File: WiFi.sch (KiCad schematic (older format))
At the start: 5 parts, among them J3 Flash enable, SW1 RESET, U9 ESP-12F

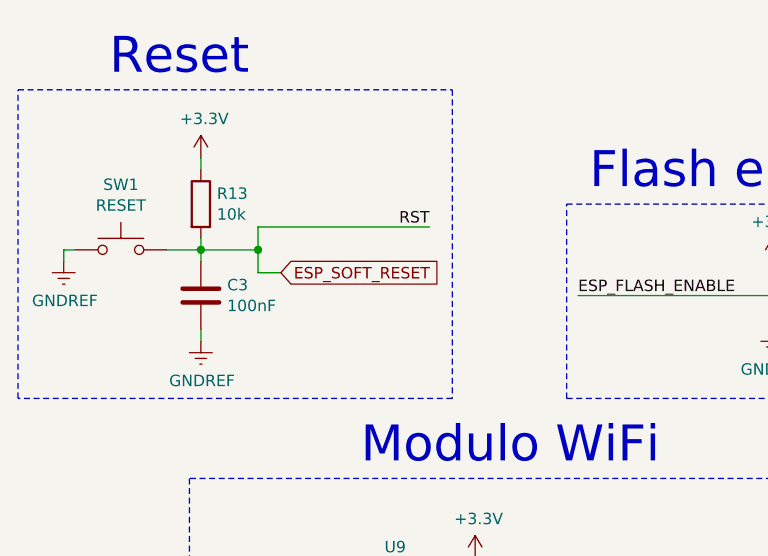
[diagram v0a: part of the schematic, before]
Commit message: Planos de tierra
Terminado el PCB con sujeciones
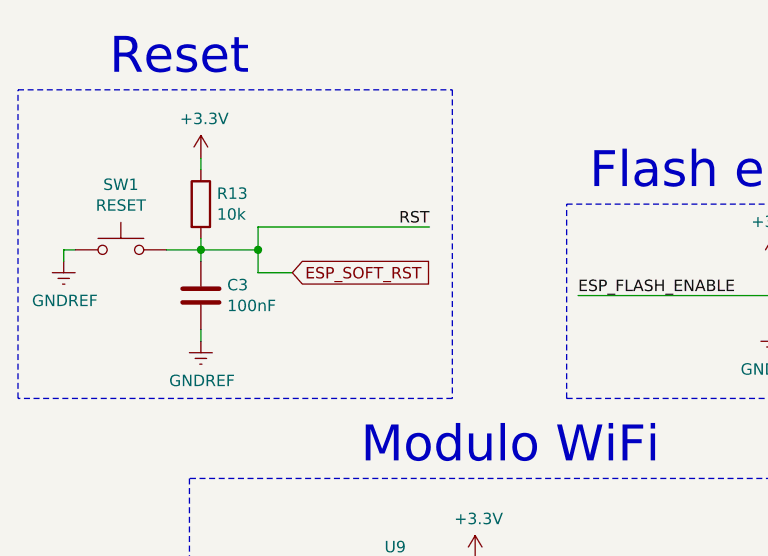
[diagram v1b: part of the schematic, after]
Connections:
- net ESP_SOFT_RESET renamed ESP_SOFT_RST
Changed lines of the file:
@@
 $Descr A4 11693 8268
 encoding utf-8
-Sheet 4 6
+Sheet 4 7
 Title "WiFi"
 Date "2021-03-03"
@@
 	4750 2600 4750 2700
 Wire Wire Line
-	4750 2700 4850 2700
+	4750 2700 4900 2700
 Connection ~ 4750 2600
-Text GLabel 4850 2700 2    50   Input ~ 0
-ESP_SOFT_RESET
+Text GLabel 4900 2700 2    50   Input ~ 0
+ESP_SOFT_RST
 Text GLabel 6450 4300 2    50   Output ~ 0
 UART_RX

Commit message: Placa terminada
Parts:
- renumbered J3 to J9, U9 to U3
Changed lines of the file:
@@
 Sheet 4 7
 Title "WiFi"
-Date "2021-03-03"
-Rev "1.0"
+Date "2021-03-30"
+Rev ""
 Comp "Crédito DyM de PCBs"
 Comment1 ""
@@
 $EndDescr
 $Comp
-L RF_Module:ESP-12F U9
+L RF_Module:ESP-12F U3
 U 1 1 6047C0A8
 P 5700 4800
-F 0 "U9" H 5350 5700 50  0000 C CNN
+F 0 "U3" H 5350 5700 50  0000 C CNN
 F 1 "ESP-12F" H 5400 5600 50  0000 C CNN
 F 2 "RF_Module:ESP-12E" H 5700 4800 50  0001 C CNN
@@
 $EndComp
 $Comp
-L power:+3.3V #PWR034
+L power:+3.3V #PWR028
 U 1 1 6047D84D
 P 5700 3950
-F 0 "#PWR034" H 5700 3800 50  0001 C CNN
+F 0 "#PWR028" H 5700 3800 50  0001 C CNN
 F 1 "+3.3V" H 5715 4123 50  0000 C CNN
 F 2 "" H 5700 3950 50  0001 C CNN
@@
 $EndComp
 $Comp
-L power:GNDREF #PWR035
+L power:GNDREF #PWR029
 U 1 1 6047EA4B
 P 5700 5550
-F 0 "#PWR035" H 5700 5300 50  0001 C CNN
+F 0 "#PWR029" H 5700 5300 50  0001 C CNN
 F 1 "GNDREF" H 5705 5377 50  0000 C CNN
 F 2 "" H 5700 5550 50  0001 C CNN
@@
 	6300 5100 6450 5100
 $Comp
-L power:GNDREF #PWR036
+L power:GNDREF #PWR030
 U 1 1 6047FB4E
 P 6450 5150
-F 0 "#PWR036" H 6450 4900 50  0001 C CNN
+F 0 "#PWR030" H 6450 4900 50  0001 C CNN
 F 1 "GNDREF" H 6455 4977 50  0000 C CNN
 F 2 "" H 6450 5150 50  0001 C CNN
@@
 P 4500 2200
 AR Path="/60476BA2/60495F55" Ref="#PWR?"  Part="1"
-AR Path="/605B052B/60495F55" Ref="#PWR032"  Part="1"
-F 0 "#PWR032" H 4500 2050 50  0001 C CNN
+AR Path="/605B052B/60495F55" Ref="#PWR026"  Part="1"
+F 0 "#PWR026" H 4500 2050 50  0001 C CNN
 F 1 "+3.3V" H 4515 2373 50  0000 C CNN
 F 2 "" H 4500 2200 50  0001 C CNN
@@
 P 3900 2650
 AR Path="/60476BA2/60495F76" Ref="#PWR?"  Part="1"
-AR Path="/605B052B/60495F76" Ref="#PWR031"  Part="1"
-F 0 "#PWR031" H 3900 2400 50  0001 C CNN
+AR Path="/605B052B/60495F76" Ref="#PWR025"  Part="1"
+F 0 "#PWR025" H 3900 2400 50  0001 C CNN
 F 1 "GNDREF" H 3905 2477 50  0000 C CNN
 F 2 "" H 3900 2650 50  0001 C CNN
@@
 P 4500 3000
 AR Path="/60476BA2/60495F7C" Ref="#PWR?"  Part="1"
-AR Path="/605B052B/60495F7C" Ref="#PWR033"  Part="1"
-F 0 "#PWR033" H 4500 2750 50  0001 C CNN
+AR Path="/605B052B/60495F7C" Ref="#PWR027"  Part="1"
+F 0 "#PWR027" H 4500 2750 50  0001 C CNN
 F 1 "GNDREF" H 4505 2827 50  0000 C CNN
 F 2 "" H 4500 3000 50  0001 C CNN
@@
 Reset
 $Comp
-L Connector_Generic:Conn_01x03 J3
+L Connector_Generic:Conn_01x03 J9
 U 1 1 6049AB82
 P 7250 2800
-F 0 "J3" H 7330 2842 50  0000 L CNN
+F 0 "J9" H 7330 2842 50  0000 L CNN
 F 1 "Flash enable" H 7330 2751 50  0000 L CNN
 F 2 "Connector_PinHeader_2.54mm:PinHeader_1x03_P2.54mm_Vertical" H 7250 2800 50  0001 C CNN
@@
 $EndComp
 $Comp
-L power:GNDREF #PWR038
+L power:GNDREF #PWR032
 U 1 1 6049C2B8
 P 7000 2950
-F 0 "#PWR038" H 7000 2700 50  0001 C CNN
+F 0 "#PWR032" H 7000 2700 50  0001 C CNN
 F 1 "GNDREF" H 7005 2777 50  0000 C CNN
 F 2 "" H 7000 2950 50  0001 C CNN
@@
 $EndComp
 $Comp
-L power:+3.3V #PWR037
+L power:+3.3V #PWR031
 U 1 1 6049CB44
 P 7000 2650
-F 0 "#PWR037" H 7000 2500 50  0001 C CNN
+F 0 "#PWR031" H 7000 2500 50  0001 C CNN
 F 1 "+3.3V" H 7015 2823 50  0000 C CNN
 F 2 "" H 7000 2650 50  0001 C CNN
